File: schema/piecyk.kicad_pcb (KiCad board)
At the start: 2 copper layers, 70 x 50 mm, 29 parts, among them IC1 ATMEGA8A-P, K1 CONN_3, K2 CONN_3, K3 CONN_4, K4 CONN_2, P1 CONN_2, P2 CONN_2, Q1 BC517, SW1 SW_edit, SW2 SW_up, SW3 SW_down, U1 78L05, U2 LM35

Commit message: Use more compact SMD components
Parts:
- removed ? (x4): , 1pin
- removed C3: 100n, R1
- removed K1, K2: CONN_3, PIN_ARRAY_3X1
- removed K3: CONN_4, PIN_ARRAY_4x1
- removed K4: CONN_2, PIN_ARRAY_2X1
- added MH: MountingHole_2-5mm_RevA_Date21Jun2010, Mounting_Holes:MountingHole_2-5mm, F.Cu at (30.8, 34.2)
- added MH: MountingHole_2-5mm_RevA_Date21Jun2010, Mounting_Holes:MountingHole_2-5mm, F.Cu at (92.8, 34.2)
- added MH: MountingHole_2-5mm_RevA_Date21Jun2010, Mounting_Holes:MountingHole_2-5mm, F.Cu at (92.8, 76.2)
- added MH: MountingHole_2-5mm_RevA_Date21Jun2010, Mounting_Holes:MountingHole_2-5mm, F.Cu at (30.8, 76.2)
- added P3: CONN_01X04, Pin_Headers:Pin_Header_Angled_1x04, F.Cu at (64.8, 107.2)
- added P4: CONN_01X04, Pin_Headers:Pin_Header_Angled_1x04, F.Cu at (51.0, 74.0)
- added P5: ISP_IDC, Pin_Headers:Pin_Header_Straight_2x05, F.Cu at (93.8, 52.2)
- added Q2: 2N7002, SMD_Packages:SOT-23-GDS, B.Cu at (75.8, 38.5)
- added Q3: BC516, Housings_TO-92:TO-92-Free-inline-wide, F.Cu at (81.8, 64.2)
- added R6: 1k, Resistors_SMD:R_0805_HandSoldering, B.Cu at (82.5, 71.2)
- added R7: 100R, Resistors_SMD:R_0805_HandSoldering, B.Cu at (77.8, 35.2)
- added RV1: 47k, Potentiometers:Potentiometer_VishaySpectrol-Econtrim-Type36P, F.Cu at (38.8, 39.2)
- added U3: HD44780, Pin_Headers:Pin_Header_Straight_1x16, F.Cu at (55.8, 34.2)
- C1, C2, C4, C5: footprint R1 -> Capacitors_SMD:C_0805_HandSoldering; moved to B.Cu
- D1: footprint LED-3MM -> LEDs:LED-3MM
- IC1: value ATMEGA8A-P -> ATMEGA8-AI; footprint DIP-28__300 -> SMD_Packages:TQFP-32; moved to B.Cu
- L1: footprint R3 -> Resistors_SMD:R_0805_HandSoldering; moved to B.Cu
- P1: value CONN_2 -> PWR_IN; footprint PIN_ARRAY_2X1 -> Connect:AK300-2
- P2: value CONN_2 -> PWR_OUT; footprint PIN_ARRAY_2X1 -> Connect:AK300-2
- Q1: value BC517 -> 2N7002; footprint TO92 -> SMD_Packages:SOT-23-GDS; moved to B.Cu
- R1: value 10k -> 22k; footprint R3 -> Resistors_SMD:R_0805_HandSoldering; moved to B.Cu
- R2, R5: value 150R -> 47R; footprint R3 -> Resistors_SMD:R_0805_HandSoldering; moved to B.Cu
- R3: value 2k2 -> 10k; footprint R3 -> Resistors_SMD:R_0805_HandSoldering; moved to B.Cu
- R4: value 550R -> 1k; footprint R3 -> Resistors_SMD:R_0805_HandSoldering; moved to B.Cu
- SW1, SW2, SW3: footprint SW_PUSH_SMALL -> Discret:SW_PUSH-12mm
- U1: footprint LM78LXX -> Discret:LM78LXX
- U2: footprint TO92-123 -> Discret:TO92-123
- moved R5 209.0 mm to (76.8, 43.2), turned to 270 degrees
- moved IC1 206.4 mm to (56.8, 53.2)
- moved D1 201.1 mm to (75.8, 72.2), turned to 180 degrees
- moved C4 199.5 mm to (66.8, 53.2)
- moved P1 194.7 mm to (31.8, 63.2), turned to 270 degrees
- moved L1 192.8 mm to (66.8, 51.0), turned to 180 degrees
- moved U1 192.7 mm to (41.8, 53.2), turned to 180 degrees
- moved C5 192.4 mm to (66.8, 55.5), turned to 0 degrees
- moved C2 191.6 mm to (46.8, 53.2), turned to 270 degrees
- moved C1 188.0 mm to (41.8, 57.2), turned to 0 degrees
- moved Q1 184.4 mm to (71.2, 68.0)
- moved P2 184.1 mm to (92.8, 63.2), turned to 270 degrees
- moved U2 183.5 mm to (63.0, 62.2), turned to 90 degrees
- moved R2 176.4 mm to (70.2, 63.5), turned to 90 degrees
- moved R1 176.2 mm to (72.2, 38.5)
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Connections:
- C1 pad 2: LCD Blight- -> GND
- C2 pad 1: Vcc +5V -> +5V
- C2 pad 2: LCD Blight- -> GND
- C4 pad 1: N-0000010 -> Net-(C4-Pad1)
- C4 pad 2: LCD Blight- -> GND
- C5 pad 1: N-0000038 -> Net-(C5-Pad1)
- C5 pad 2: LCD Blight- -> GND
- D1 pad 1: N-0000013 -> Net-(D1-Pad1)
- D1 pad 2: LCD Blight- -> Net-(D1-Pad2)
- IC1 pad 1: N-0000032 -> /K_dn
- IC1 pad 10: LCD data4 -> /LCD_Data4
- IC1 pad 11: LCD data5 -> /LCD_Data5
- IC1 pad 12: LCD data6 -> /LCD_Data6
- IC1 pad 13: LCD data7 -> /LCD_Data7
- IC1 pad 14: LCD en -> /LCD_Blight_PWM
- IC1 pad 15: LCD rw -> /MOSI
- IC1 pad 16: LCD rs -> /MISO
- IC1 pad 17: (no net) -> /SCK
- IC1 pad 18: (no net) -> Net-(C4-Pad1)
- IC1 pad 19: (no net) -> Net-(IC1-Pad19)
- IC1 pad 2: N-0000016 -> Net-(IC1-Pad2)
- IC1 pad 20: N-0000010 -> Net-(C5-Pad1)
- IC1 pad 21: N-0000038 -> GND
- IC1 pad 22: LCD Blight- -> Net-(IC1-Pad22)
- IC1 pad 23: N-0000012 -> Net-(IC1-Pad23)
- IC1 pad 24: (no net) -> Net-(IC1-Pad24)
- IC1 pad 25: (no net) -> Net-(IC1-Pad25)
- IC1 pad 26: (no net) -> Net-(IC1-Pad26)
- IC1 pad 27: (no net) -> Net-(IC1-Pad27)
- IC1 pad 28: (no net) -> Net-(IC1-Pad28)
- IC1 pad 3: N-0000015 -> GND
- IC1 pad 4: N-0000027 -> +5V
- IC1 pad 5: N-0000030 -> GND
- IC1 pad 6: N-0000026 -> +5V
- IC1 pad 7: Vcc +5V -> /LCD_RS
- IC1 pad 8: LCD Blight- -> /LCD_RW
- IC1 pad 9: (no net) -> /LCD_EN
- L1 pad 1: Vcc +5V -> +5V
- L1 pad 2: N-0000010 -> Net-(C4-Pad1)
- P1 pad 2: LCD Blight- -> GND
- P2 pad 1: +12V / heating - -> PWR
- P2 pad 2: +12V -> GND
- R1 pad 1: Vcc +5V -> +5V
- R1 pad 2: N-0000032 -> /RST
- R2 pad 1: N-0000016 -> Net-(Q1-PadG)
- R2 pad 2: N-000009 -> Net-(IC1-Pad30)
- R3 pad 1: Vcc +5V -> GND
- R3 pad 2: LCD Contr -> Net-(IC1-Pad30)
- R4 pad 1: Vcc +5V -> +12V
- R4 pad 2: LCD Blight+ -> Net-(D1-Pad1)
- R5 pad 1: N-0000015 -> Net-(Q2-PadG)
- R5 pad 2: N-0000013 -> /LCD_Blight_PWM
- SW1 pad 1: N-0000026 -> /K_edit
- SW1 pad 2: LCD Blight- -> Net-(P3-Pad4)
- SW2 pad 1: N-0000030 -> /K_up
- SW2 pad 2: LCD Blight- -> Net-(P3-Pad4)
- SW3 pad 1: N-0000027 -> /K_dn
- SW3 pad 2: LCD Blight- -> Net-(P3-Pad4)
- U1 pad GND: LCD Blight- -> GND
- U1 pad VO: Vcc +5V -> +5V
- U2 pad 1: Vcc +5V -> +5V
- U2 pad 2: N-0000012 -> GND
- U2 pad 3: LCD Blight- -> Net-(IC1-Pad23)
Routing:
- net +5V: track 0.00 -> 146.5 mm
- net Vcc +5V: track 86.0 -> 0.00 mm, vias 2 -> 0
- net /RST: track 0.00 -> 71.2 mm, vias 0 -> 4
- net N-0000015: track 60.8 -> 0.00 mm
- net /MOSI: track 0.00 -> 45.3 mm, vias 0 -> 2
- net N-0000016: track 40.6 -> 0.00 mm, vias 2 -> 0
- net /MISO: track 0.00 -> 40.0 mm, vias 0 -> 2
- net /SCK: track 0.00 -> 33.6 mm, vias 0 -> 2
- net LCD data4: track 30.0 -> 0.00 mm
- net /LCD_Blight_PWM: track 0.00 -> 29.8 mm
- net LCD data5: track 26.4 -> 0.00 mm
- net /LCD_Data7: track 0.00 -> 24.4 mm
- net +12V / heating -: track 23.0 -> 0.00 mm
- net /LCD_Data6: track 0.00 -> 22.8 mm
- net LCD data6: track 22.8 -> 0.00 mm
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- added copper zone on B.Cu, net GND
- removed copper zone on B.Cu, net LCD Blight-
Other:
- net class Default: clearance 0.4 -> 0.3; via_drill 1 -> 0.7
- net class PWR added: clearance 0.5, trace_width 1, via_dia 2, via_drill 0.7
- rule trace_clearance: 0.4 -> 0.3
- rule trace_min: 0.254 -> 0.3
- rule via_min_drill: 0.508 -> 0.5
- rule via_min_size: 0.889 -> 1
- board text added: "piecyk 1.0"
- board text removed: "piecyk"

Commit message: Add 10uF capacitor, optimalize PCB layout
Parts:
- added C3: 10u, Capacitors_Tantalum_SMD:TantalC_SizeA_EIA-3216_HandSoldering, B.Cu at (42.8, 54.0)
- moved C1 5.34 mm to (36.5, 58.2)
- moved U1 5.26 mm to (36.5, 53.0)
- moved C2 1.46 mm to (45.5, 54.0)
- moved C5 0.79 mm to (67.5, 55.2)
- moved C4 0.75 mm to (67.5, 53.2)
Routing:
- net +5V: track 146.5 -> 157.4 mm
- net /LCD_EN: track 16.1 -> 20.5 mm
- net /K_dn: track 19.4 -> 22.5 mm
- net /RST: track 71.2 -> 69.0 mm
- net /LCD_Data5: track 21.1 -> 19.5 mm
- net /LCD_Data4: track 19.4 -> 17.8 mm
- net /LCD_Data6: track 22.8 -> 21.2 mm
- net /LCD_Data7: track 24.4 -> 22.9 mm

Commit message: Add I/O markings to the PCB
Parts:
- R6: value 1k -> 2k2
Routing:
- net /LCD_RW: track 22.0 -> 25.2 mm
- net +5V: track 157.4 -> 160.0 mm
- net /LCD_RS: track 22.3 -> 24.5 mm
- net Net-(RV1-Pad2): track 8.96 -> 7.85 mm
- net /SCK: track 33.6 -> 34.3 mm
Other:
- board text added: "+"
- board text added: "in"
- board text added: "out"

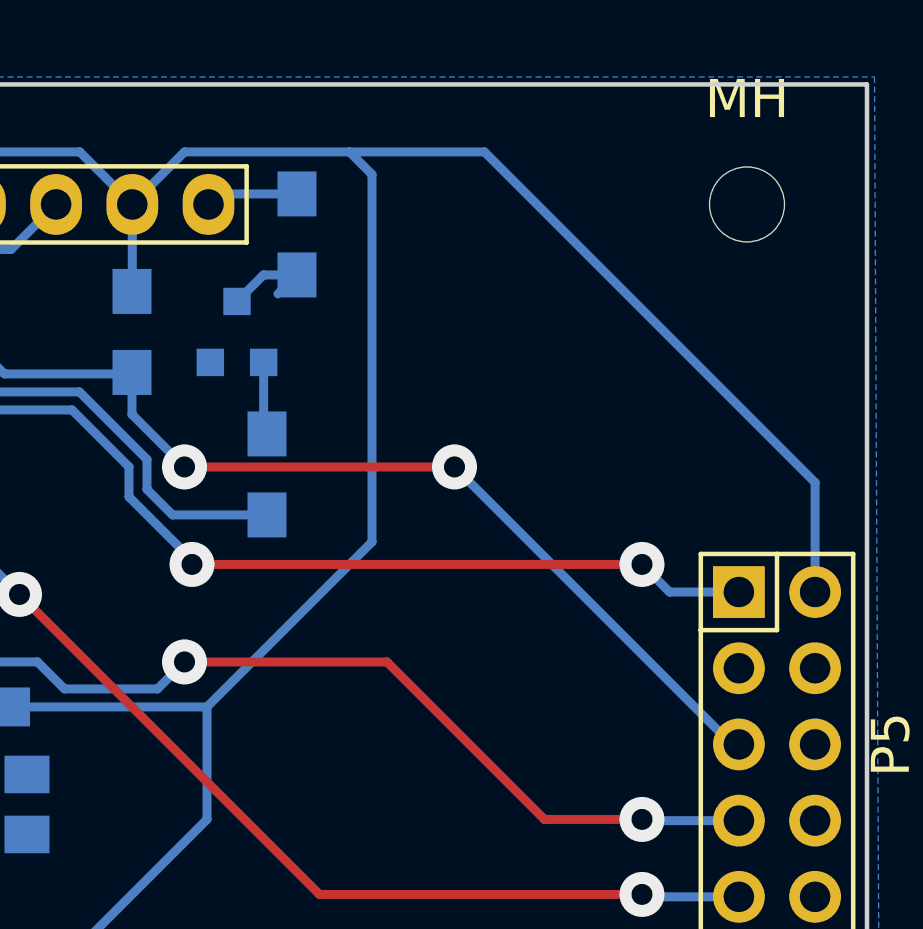
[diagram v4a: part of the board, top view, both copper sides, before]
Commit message: Add missing pull-down resistor, adjust brightness levels
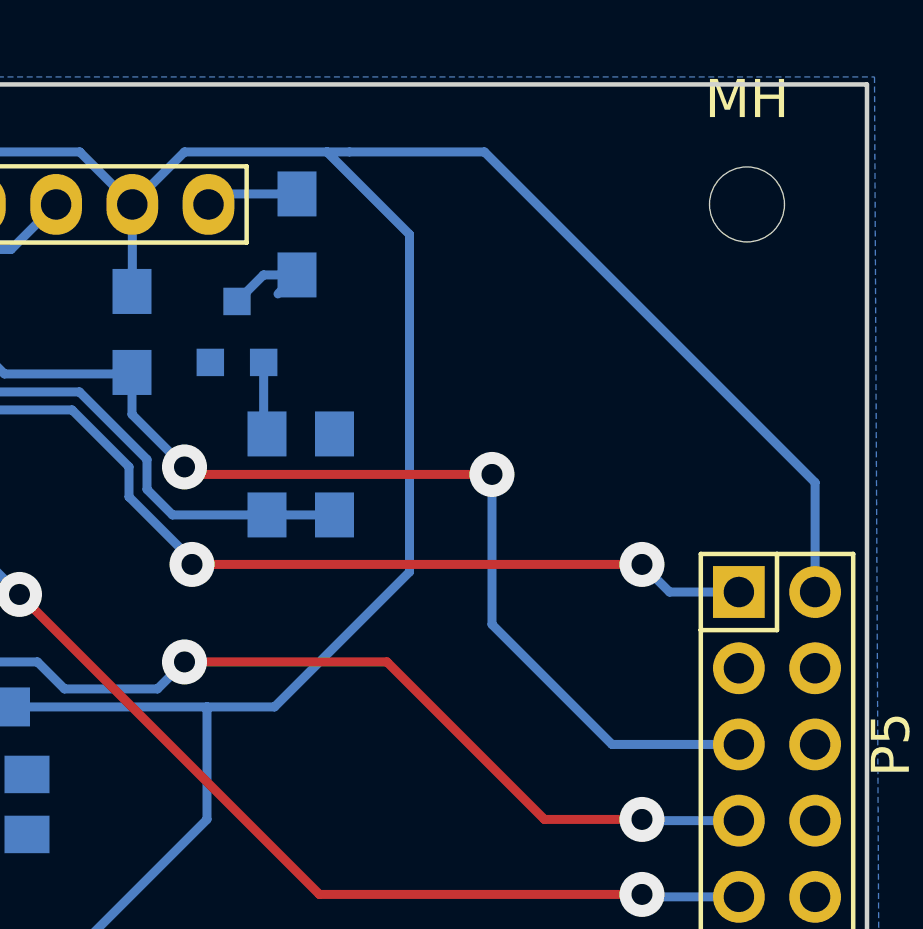
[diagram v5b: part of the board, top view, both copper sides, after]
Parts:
- added R8: 10k, Resistors_SMD:R_0805_HandSoldering, B.Cu at (79.0, 43.2)
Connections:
- IC1 pad 1: /K_dn -> /K_edit
- IC1 pad 31: /K_edit -> /K_up
- IC1 pad 32: /K_up -> /K_dn
- P4 pad 1: /K_edit -> /K_up
- P4 pad 2: /K_up -> /K_dn
- P4 pad 3: /K_dn -> /K_edit
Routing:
- net /K_edit: track 16.0 -> 22.5 mm, vias 0 -> 2
- net /K_dn: track 22.5 -> 16.6 mm, vias 2 -> 0
- net /RST: track 69.0 -> 72.2 mm
- net +5V: track 160.0 -> 162.6 mm
- net /LCD_Blight_PWM: track 29.8 -> 32.0 mm
- net /K_up: track 16.6 -> 16.0 mm
